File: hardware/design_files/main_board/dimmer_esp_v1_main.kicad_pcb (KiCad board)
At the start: 4 copper layers, 44 x 48.1 mm, 55 parts, among them IC1 PEC11S-929K-S0015, J1 Screw_Terminal_01x03, J2 SM05B-SRSS-TB_LF__SN_, J3 Conn_01x02, K1 FTR-LYCA005Y, Q1 BC817, SW1 Commission, SW2 Toggle, SW3 Reset, U1 SGM2212-3.3XKC3G/TR, U2 USB TYPE-C 16PLT-H10.0, U3 SN74LV1T125DBVR, U4 ESP32-C6-MINI

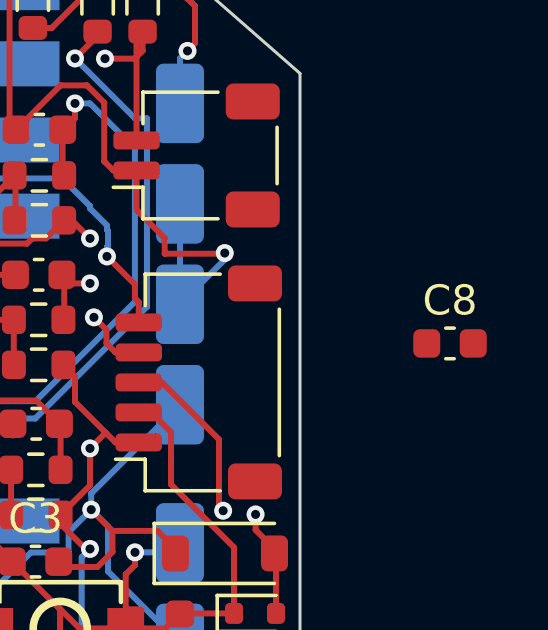
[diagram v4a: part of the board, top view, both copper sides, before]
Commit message: Remove bypass cap for LED for now (no space on PCB)
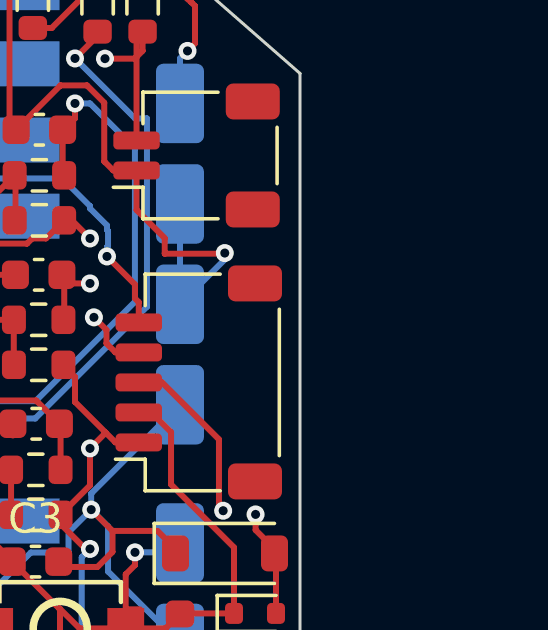
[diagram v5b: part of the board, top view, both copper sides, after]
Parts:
- removed C8: 0.1uF, Capacitor_SMD:C_0603_1608Metric
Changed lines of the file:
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@@
-		)
-	)
-	(footprint "Capacitor_SMD:C_0603_1608Metric"
-		(layer "F.Cu")
-		(at 194.5 55)
-		(descr "Capacitor SMD 0603 (1608 Metric), square (rectangular) end terminal, IPC-7351 nominal, (Body size source: IPC-SM-782 page 76, https://www.pcb-3d.com/wordpress/wp-content/uploads/ipc-sm-782a_amendment_1_and_2.pdf), generated with kicad-footprint-generator")
-		(tags "capacitor")
-		(property "Reference" "C8"
-			(at 0 -1.43 0)
-			(layer "F.SilkS")
-			(effects
-				(font
-					(size 1 1)
-					(thickness 0.15)
-				)
-			)
-		)
-		(property "Value" "0.1uF"
-			(at 0 1.43 0)
-			(layer "F.Fab")
-			(effects
-				(font
-					(size 1 1)
-					(thickness 0.15)
-				)
-			)
-		)
-		(property "Datasheet" "~"
-			(at 0 0 0)
-			(layer "F.Fab")
-			(hide yes)
-			(effects
-				(font
-					(size 1.27 1.27)
-					(thickness 0.15)
-				)
-			)
-		)
-		(property "Description" "WS2812B VDD bypass capacitor"
-			(at 0 0 0)
-			(layer "F.Fab")
-			(hide yes)
-			(effects
-				(font
-					(size 1.27 1.27)
-					(thickness 0.15)
-				)
-			)
-		)
-		(property "LCSC" "C14663"
-			(at 0 0 0)
-			(unlocked yes)
-			(layer "F.Fab")
-			(hide yes)
-			(effects
-				(font
-					(size 1 1)
-					(thickness 0.15)
-				)
-			)
-		)
-		(property ki_fp_filters "C_*")
-		(sheetname "/")
-		(sheetfile "dimmer_esp_v1_main.kicad_sch")
-		(attr smd)
-		(fp_line
-			(start -0.14058 -0.51)
-			(end 0.14058 -0.51)
-			(stroke
-				(width 0.12)
-				(type solid)
-			)
-			(layer "F.SilkS")
-		)
-		(fp_line
-			(start -0.14058 0.51)
-			(end 0.14058 0.51)
-			(stroke
-				(width 0.12)
-				(type solid)
-			)
-			(layer "F.SilkS")
-		)
-		(fp_line
-			(start -1.48 -0.73)
-			(end 1.48 -0.73)
-			(stroke
-				(width 0.05)
-				(type solid)
-			)
-			(layer "F.CrtYd")
-		)
-		(fp_line
-			(start -1.48 0.73)
-			(end -1.48 -0.73)
-			(stroke
-				(width 0.05)
-				(type solid)
-			)
-			(layer "F.CrtYd")
-		)
-		(fp_line
-			(start 1.48 -0.73)
-			(end 1.48 0.73)
-			(stroke
-				(width 0.05)
-				(type solid)
-			)
-			(layer "F.CrtYd")
-		)
-		(fp_line
-			(start 1.48 0.73)
-			(end -1.48 0.73)
-			(stroke
-				(width 0.05)
-				(type solid)
-			)
-			(layer "F.CrtYd")
-		)
-		(fp_line
-			(start -0.8 -0.4)
-			(end 0.8 -0.4)
-			(stroke
-				(width 0.1)
-				(type solid)
-			)
-			(layer "F.Fab")
-		)
-		(fp_line
-			(start -0.8 0.4)
-			(end -0.8 -0.4)
-			(stroke
-				(width 0.1)
-				(type solid)
-			)
-			(layer "F.Fab")
-		)
-		(fp_line
-			(start 0.8 -0.4)
-			(end 0.8 0.4)
-			(stroke
-				(width 0.1)
-				(type solid)
-			)
-			(layer "F.Fab")
-		)
-		(fp_line
-			(start 0.8 0.4)
-			(end -0.8 0.4)
-			(stroke
-				(width 0.1)
-				(type solid)
-			)
-			(layer "F.Fab")
-		)
-		(fp_text user "${REFERENCE}"
-			(at 0 0 0)
-			(layer "F.Fab")
-			(effects
-				(font
-					(size 0.4 0.4)
-					(thickness 0.06)
-				)
-			)
-		)
-		(pad "1" smd roundrect
-			(at -0.775 0)
-			(size 0.9 0.95)
-			(layers "F.Cu" "F.Mask" "F.Paste")
-			(roundrect_rratio 0.25)
-			(net 1 "GND")
-			(pintype "passive")
-		)
-		(pad "2" smd roundrect
-			(at 0.775 0)
-			(size 0.9 0.95)
-			(layers "F.Cu" "F.Mask" "F.Paste")
-			(roundrect_rratio 0.25)
-			(net 28 "+5V")
-			(pintype "passive")
-		)
-		(embedded_fonts no)
-		(model "${KICAD9_3DMODEL_DIR}/Capacitor_SMD.3dshapes/C_0603_1608Metric.step"
-			(offset
-				(xyz 0 0 0)
-			)
-			(scale
-				(xyz 1 1 1)
-			)
-			(rotate
-				(xyz 0 0 0)
-			)
 		)
 	)
